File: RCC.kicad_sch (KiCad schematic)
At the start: 18 parts, among them J1 Conn_01x02, J2 USB_C_Receptacle_USB2.0_16P, U1 BQ24040DGQR, U2 ESD7104MUTAG, U3 TLV75801PDRV

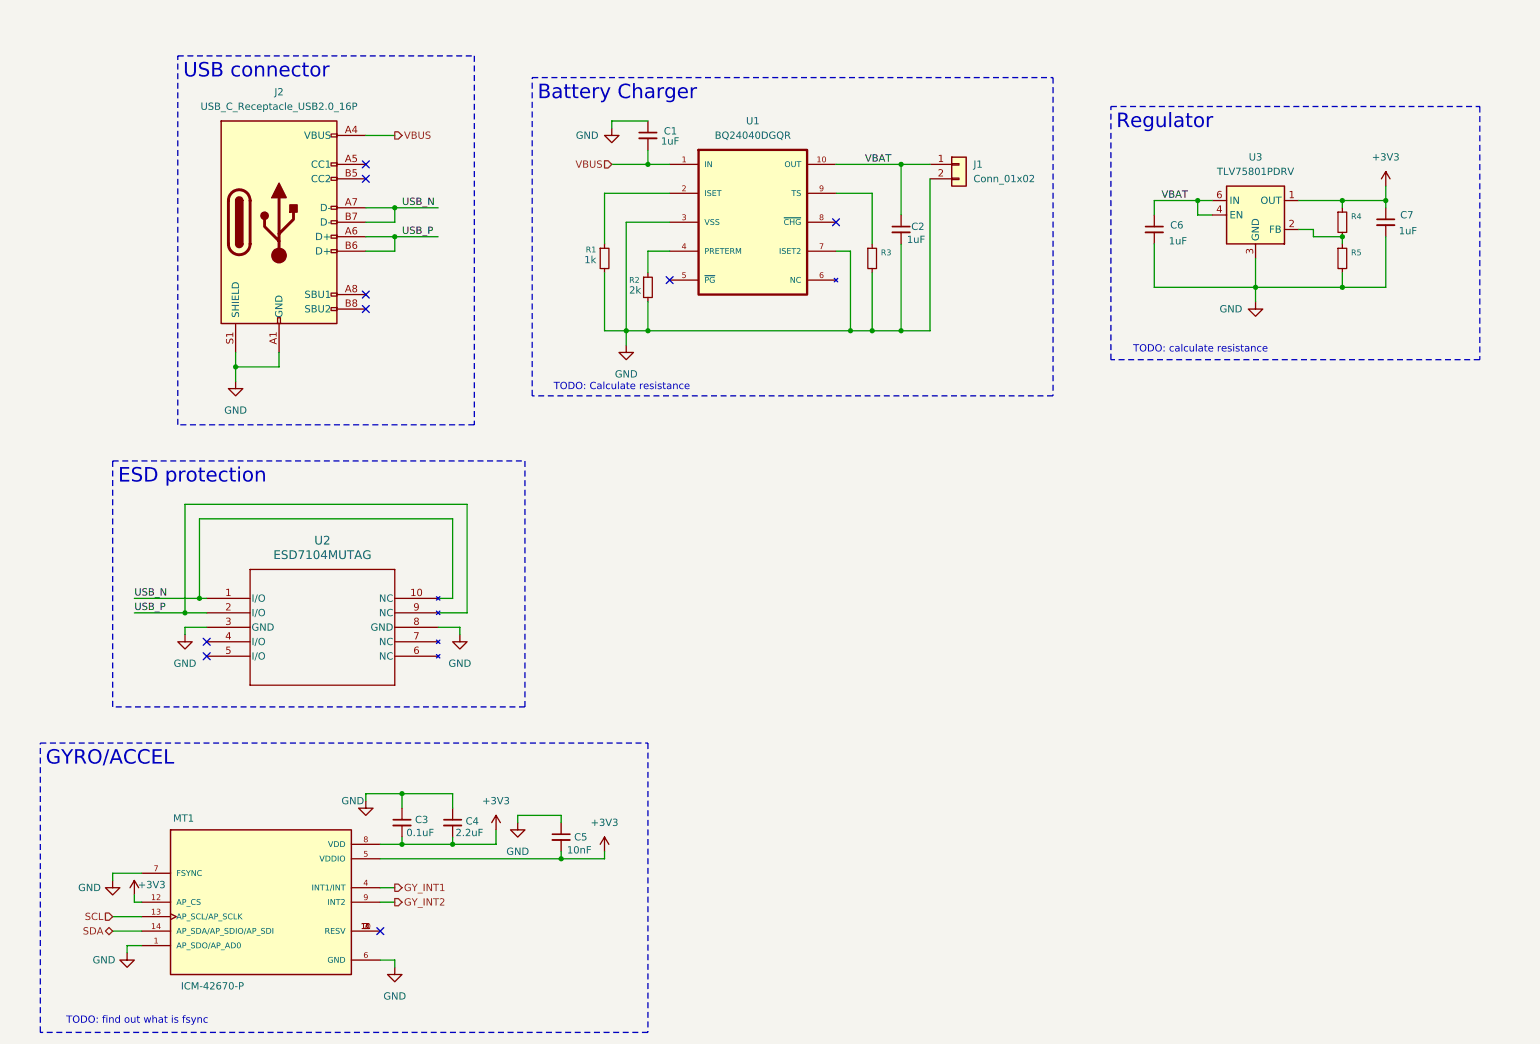
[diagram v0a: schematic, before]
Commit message: Add microcontroller and display to schematic
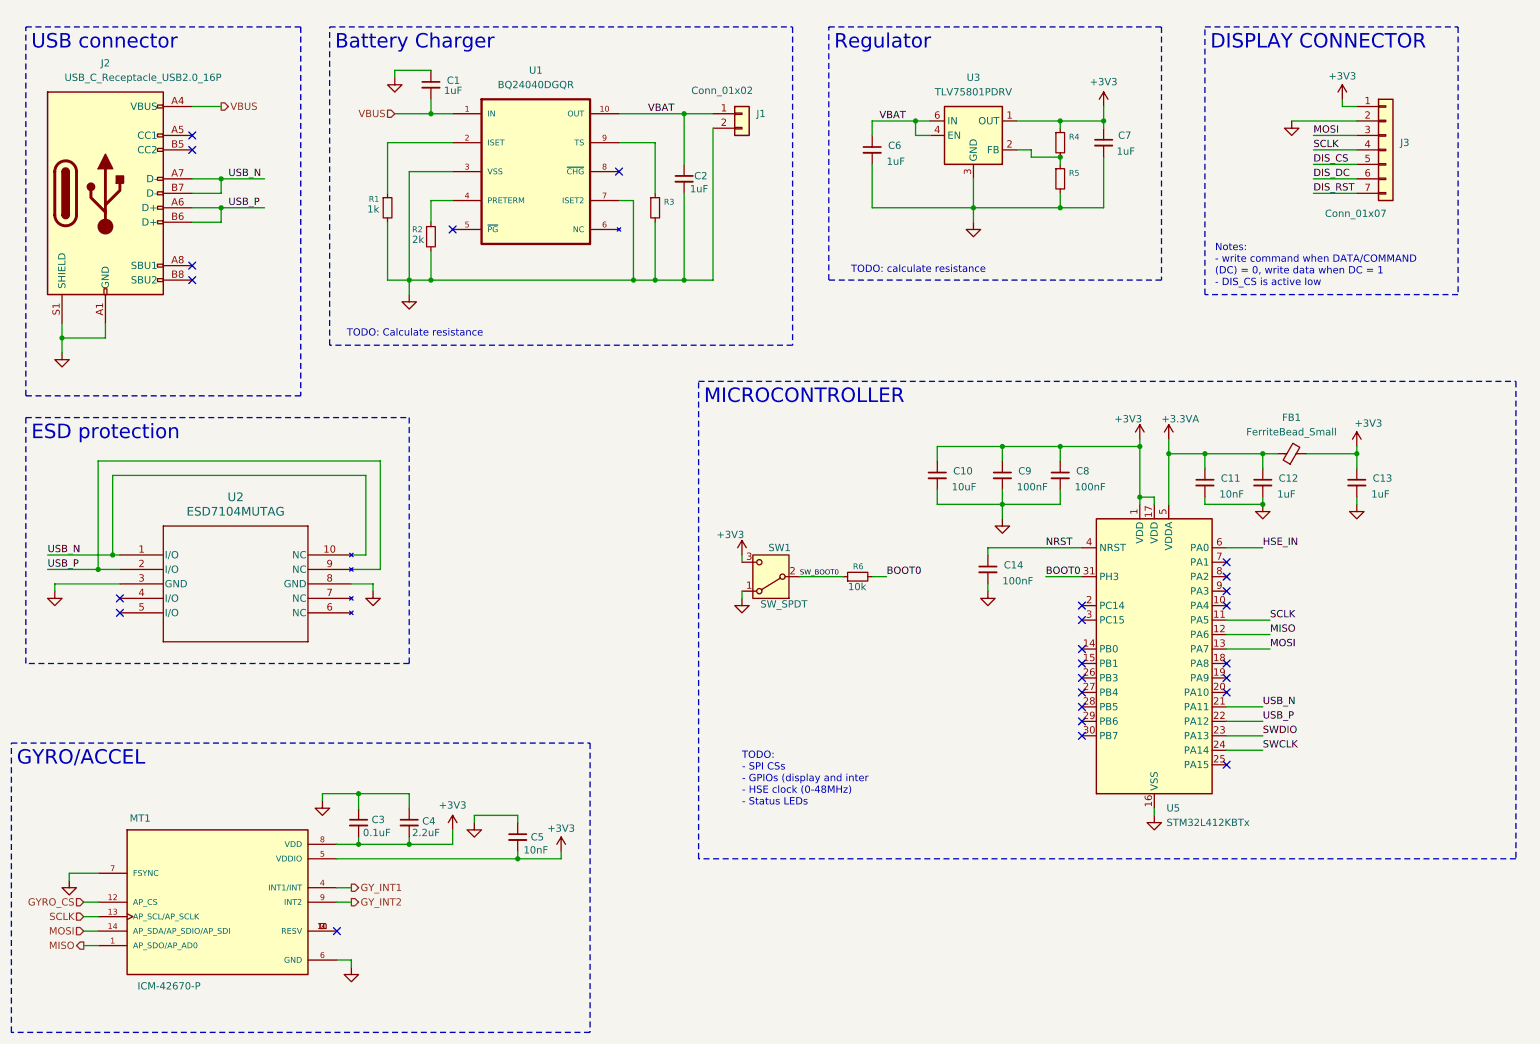
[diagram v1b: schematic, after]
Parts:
- added C10: 10uF, Capacitor_SMD:C_0603_1608Metric, symbol Device:C_Small
- added C11: 10nF, Capacitor_SMD:C_0603_1608Metric, symbol Device:C_Small
- added C12, C13: 1uF, Capacitor_SMD:C_0603_1608Metric, symbol Device:C_Small
- added C14, C8, C9: 100nF, Capacitor_SMD:C_0603_1608Metric, symbol Device:C_Small
- added FB1: FerriteBead_Small, symbol Device:FerriteBead_Small
- added J3: Conn_01x07, Connector_JST:JST_EH_S7B-EH_1x07_P2.50mm_Horizontal, symbol Connector_Generic:Conn_01x07
- added R6: 10k, Resistor_SMD:R_0603_1608Metric, symbol Device:R_Small
- added SW1: SW_SPDT, symbol Switch:SW_SPDT
- added U5: STM32L412KBTx, Package_QFP:LQFP-32_7x7mm_P0.8mm, symbol MCU_ST_STM32L4:STM32L412KBTx
- MT1: footprint ICM-42670-P:XDCR_ICM-42670-P -> ICM42670:XDCR_ICM-42670-P
- R3, R4, R5: footprint (none) -> Resistor_SMD:R_0603_1608Metric
- U2: footprint UDFN10_ONS -> ESD7104:UDFN10_ONS
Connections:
- net +3V3: now also C10.1, C13.1, C8.1, C9.1, FB1.2, J3.1 (Pin_1), SW1.3 (C), U5.1 (VDD), U5.17 (VDD); no longer MT1.12 (AP_CS)
- net GND: now also C10.2, C11.2, C12.2, C13.2, C14.2, C8.2, C9.2, J3.2 (Pin_2), SW1.1 (A), U5.16 (VSS), U5.32 (VSS); no longer MT1.1 (AP_SDO/AP_AD0)
- net USB_N: now also U5.21 (PA11)
- net USB_P: now also U5.22 (PA12)
- net SCL renamed SCLK
- net SCLK: now also J3.4 (Pin_4), U5.11 (PA5)
- net SDA renamed MOSI
- net MOSI: now also J3.3 (Pin_3), U5.13 (PA7)
- new net +3.3VA: C11.1, C12.1, FB1.1, U5.5 (VDDA)
- new net BOOT0: R6.2, U5.31 (PH3)
- new net DIS_CS: J3.5 (Pin_5)
- new net DIS_DC: J3.6 (Pin_6)
- new net DIS_RST: J3.7 (Pin_7)
- new net GYRO_CS: MT1.12 (AP_CS)
- new net HSE_IN: U5.6 (PA0)
- new net MISO: MT1.1 (AP_SDO/AP_AD0), U5.12 (PA6)
- new net NRST: C14.1, U5.4 (NRST)
- new net SWCLK: U5.24 (PA14)
- new net SWDIO: U5.23 (PA13)
- new net SW_BOOT0: R6.1, SW1.2 (B)
- no-connect marks 9 -> 26
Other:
- note added: "Notes: - write command when DATA/COMMAND (DC) = 0, write data when DC = 1 - DIS_CS is active low"
- note added: "TODO: - SPI CSs - GPIOs (display and inter - HSE clock (0-48MHz) - Status LEDs"
- note removed: "TODO: find out what is fsync"
- moved on the sheet: C1, C2, C3, C4, C5, C6, C7, J1, J2, MT1, R1, R2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

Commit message: Add resistor value for regulator and pull up resistor and debug connector for microcontroller
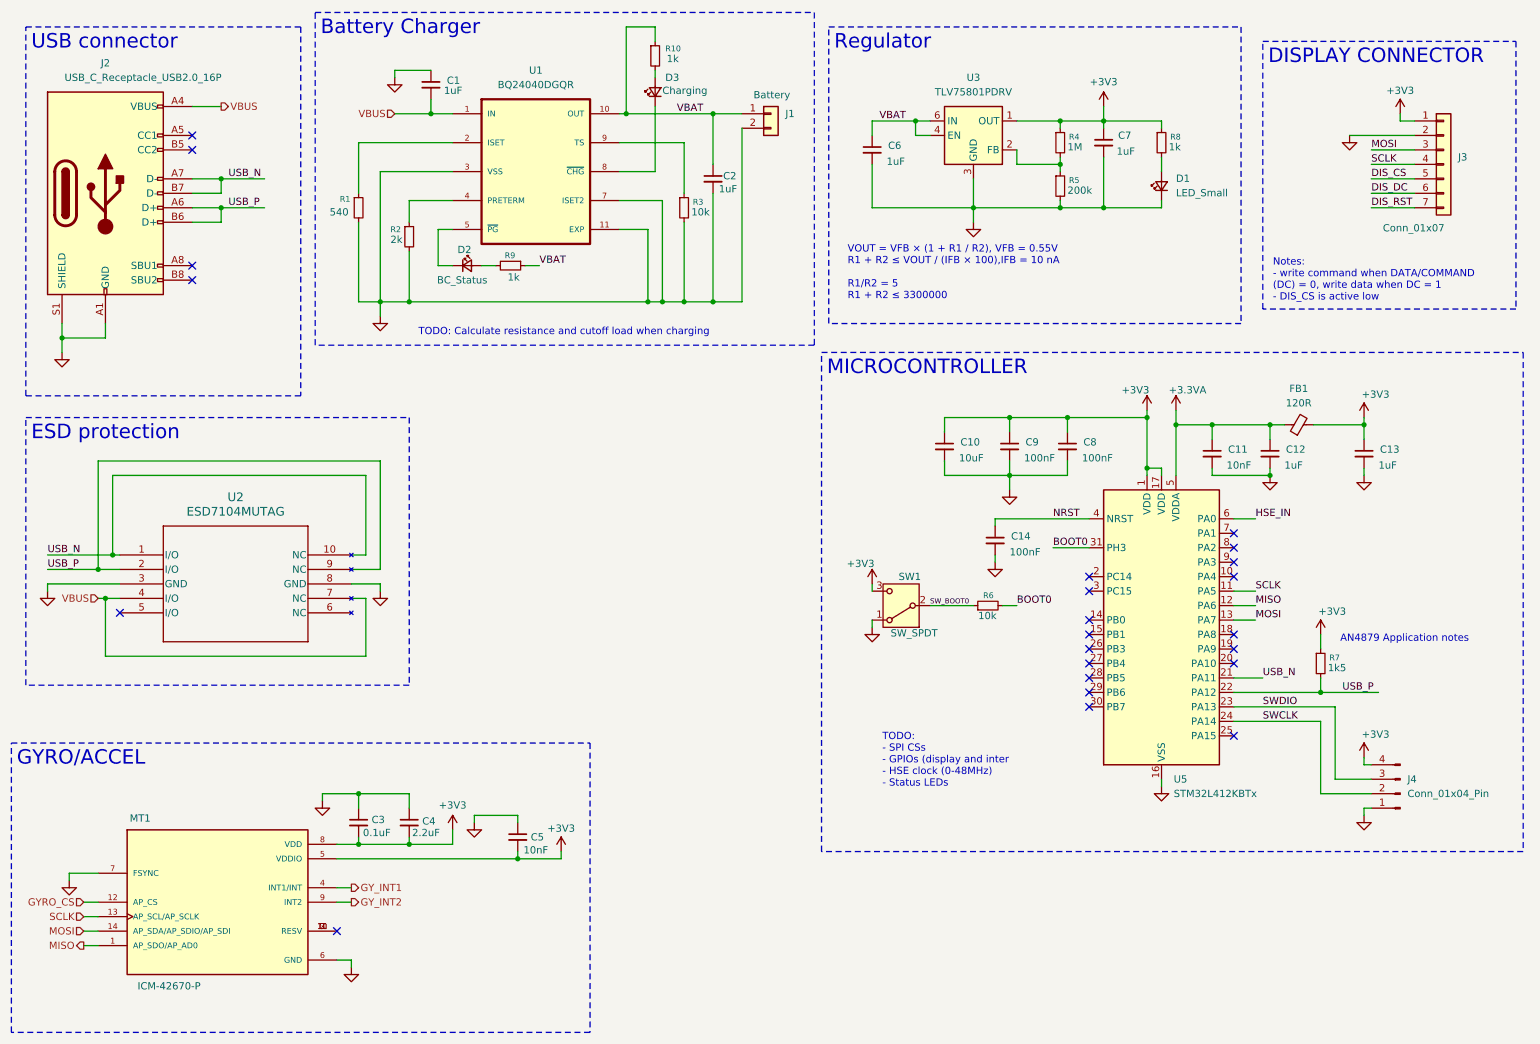
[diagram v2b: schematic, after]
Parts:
- removed U1: BQ24040DGQR, BQ24040DSQR:SON40P200X200X80-11N, symbol BQ24050DGQR:BQ24040DGQR
- added D1: LED_Small, LED_SMD:LED_0603_1608Metric, symbol Device:LED_Small
- added D2: BC_Status, LED_SMD:LED_0603_1608Metric, symbol Device:LED_Small
- added D3: Charging, LED_SMD:LED_0603_1608Metric, symbol Device:LED_Small
- added J4: Conn_01x04_Pin, symbol Connector:Conn_01x04_Pin
- added R10, R8, R9: 1k, Resistor_SMD:R_0603_1608Metric, symbol Device:R_Small
- added R7: 1k5, Resistor_SMD:R_0603_1608Metric, symbol Device:R_Small
- added U1: BQ24040DGQR, BQ24040DSQR:SON40P200X200X80-11N, symbol BQ24040DGQR:BQ24040DGQR
- FB1: value FerriteBead_Small -> 120R; footprint (none) -> Inductor_SMD:L_0603_1608Metric
- J1: value Conn_01x02 -> Battery
- R1: value 1k -> 540
- R3: value ~ -> 10k
- R4: value ~ -> 1M
- R5: value ~ -> 200k
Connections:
- net +3V3: now also J4.4 (Pin_4), R7.1, R8.1
- net GND: now also D1.1 (K), J4.1 (Pin_1), U1.11 (EXP), U1.3 (VSS), U1.7 (ISET2)
- net SWCLK: now also J4.2 (Pin_2)
- net SWDIO: now also J4.3 (Pin_3)
- net USB_P: now also R7.2
- net VBAT: now also R10.1, R9.1, U1.10 (OUT)
- net VBUS: now also U2.4 (I/O), U2.7 (NC), U1.1 (IN)
- net at R2.1: now also U1.4 (PRETERM)
- net at R1.1: now also U1.2 (ISET)
- net at R3.1: now also U1.9 (TS)
- new net: D2.1 (K), U1.5 (~{PG})
- new net: D2.2 (A), R9.2
- new net: D1.2 (A), R8.2
- new net: D3.2 (A), R10.2
- new net: D3.1 (K), U1.8 (~{CHG})
- no-connect marks 26 -> 23
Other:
- note added: "AN4879 Application notes"
- note added: "TODO: Calculate resistance and cutoff load when charging"
- note added: "VOUT = VFB × (1 + R1 / R2), VFB = 0.55V R1 + R2 ≤ VOUT / (IFB × 100),IFB = 10 nA R1/R2 = 5 R1 + R2 ≤ 3300000"
- note removed: "TODO: Calculate resistance"
- note removed: "TODO: calculate resistance"
- moved on the sheet: C10, C11, C12, C13, C14, C2, C8, C9, FB1, J1, J3, R1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

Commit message: Initial PCB layout
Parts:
- removed R2: 2k, Resistor_SMD:R_0603_1608Metric, symbol Device:R_Small
- removed R3: 10k, Resistor_SMD:R_0603_1608Metric, symbol Device:R_Small
- removed SW1: SW_SPDT, symbol Switch:SW_SPDT
- added C15: 100nF, Capacitor_SMD:C_0603_1608Metric, symbol Device:C_Small
- added H1, H2, H3, H4: MountingHole, MountingHole:MountingHole_3.2mm_M3, symbol Mechanical:MountingHole
- added R11: 0, Resistor_SMD:R_0603_1608Metric, symbol Device:R_Small
- added SW2: SW_Push, Button_Switch_SMD:SW_Push_1P1T_NO_CK_KMR2, symbol Switch:SW_Push
- J2: footprint (none) -> Connector_USB:USB_C_Receptacle_G-Switch_GT-USB-7010ASV
- J4: footprint (none) -> Connector_JST:JST_EH_B4B-EH-A_1x04_P2.50mm_Vertical
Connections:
- net +3V3: now also J4.1 (Pin_1), SW2.2; no longer J4.4 (Pin_4)
- net GND: now also J4.4 (Pin_4), C15.2, R11.2; no longer J2.S1 (SHIELD), J4.1 (Pin_1)
- net SWCLK: now also J4.3 (Pin_3); no longer J4.2 (Pin_2)
- net SWDIO: now also J4.2 (Pin_2); no longer J4.3 (Pin_3)
- net SW_BOOT0: now also C15.1, SW2.1
- net CHG_STATUS: now reaches D3.1 (K), U1.8 (~{CHG})
- new net: J2.S1 (SHIELD), R11.1
- no-connect marks 23 -> 25
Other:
- note added: "Connect CC line? 5k11"
- note added: "Display mount are M3 Display dimension: 44.5mm x 37mm"
- moved on the sheet: D3, J4, R10, R6

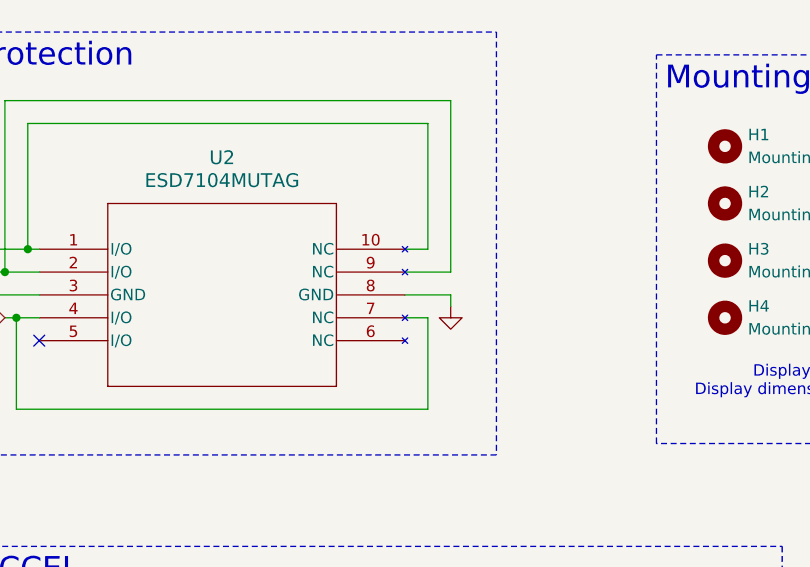
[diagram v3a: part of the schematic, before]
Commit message: Change PCB stackup to 4 layer
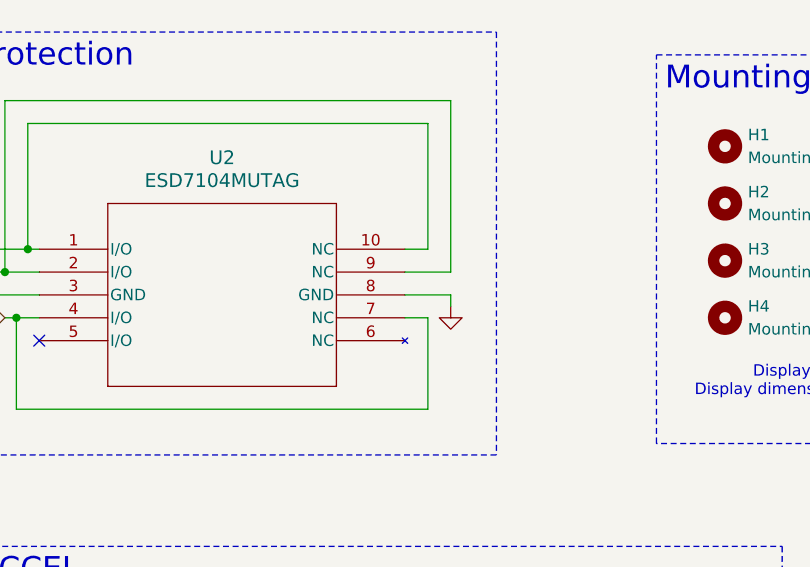
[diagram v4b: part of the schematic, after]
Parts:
- SW2: Link (none) -> https://www.digikey.com.au/en/products/detail/c-k/PTS636SM4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
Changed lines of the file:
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@@
+			)
+		)
+		(property "Link" "https://www.digikey.com.au/en/products/detail/c-k/PTS636SM43SMTR-LFS/10071723?_gl=1*1en786n*_up*MQ..*_gs*NA..&gclid=CjwKCAjw3f_BBhAPEiwAaA3K5EzdtylBuzTH5Tp0Lw0_r2Jmw2ftEDYT3LvE-E-vyVXnVc6dkaUpDRoCz0sQAvD_BwE&gclsrc=aw.ds&gbraid=0AAAAADrbLliRg89CaQ4Hkh6Tuyu0avDiE"
+			(at 172.72 116.84 0)
+			(effects
+				(font
+					(size 1.27 1.27)
+				)
+				(hide yes)
 			)
 		)
